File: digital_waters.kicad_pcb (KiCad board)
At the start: 4 copper layers, 100 x 45 mm, 118 parts, among them J1 Conn_Batt, J11 ESP32 [R], J16 ESP32 [L], J18 EZO Carrier Board, J2 Conn_Remote, J3 Conn_Sense_A, J4 Conn_Sense_B, J5 Conn_Illum, J6 Cal_in, U1 MCP3208, U10 ST485E, U12 DHT20, U13 TLV4387, U14 MCP1727-5002xSN, U15 TLV4387, U16 AP63200WU, U2 M24C02-FMN, U3 OPA197xD, U5 DIO5661ST6, U6 TPS22929D, U7 REF3040, U8 REF3025, U9 TLV2387DR

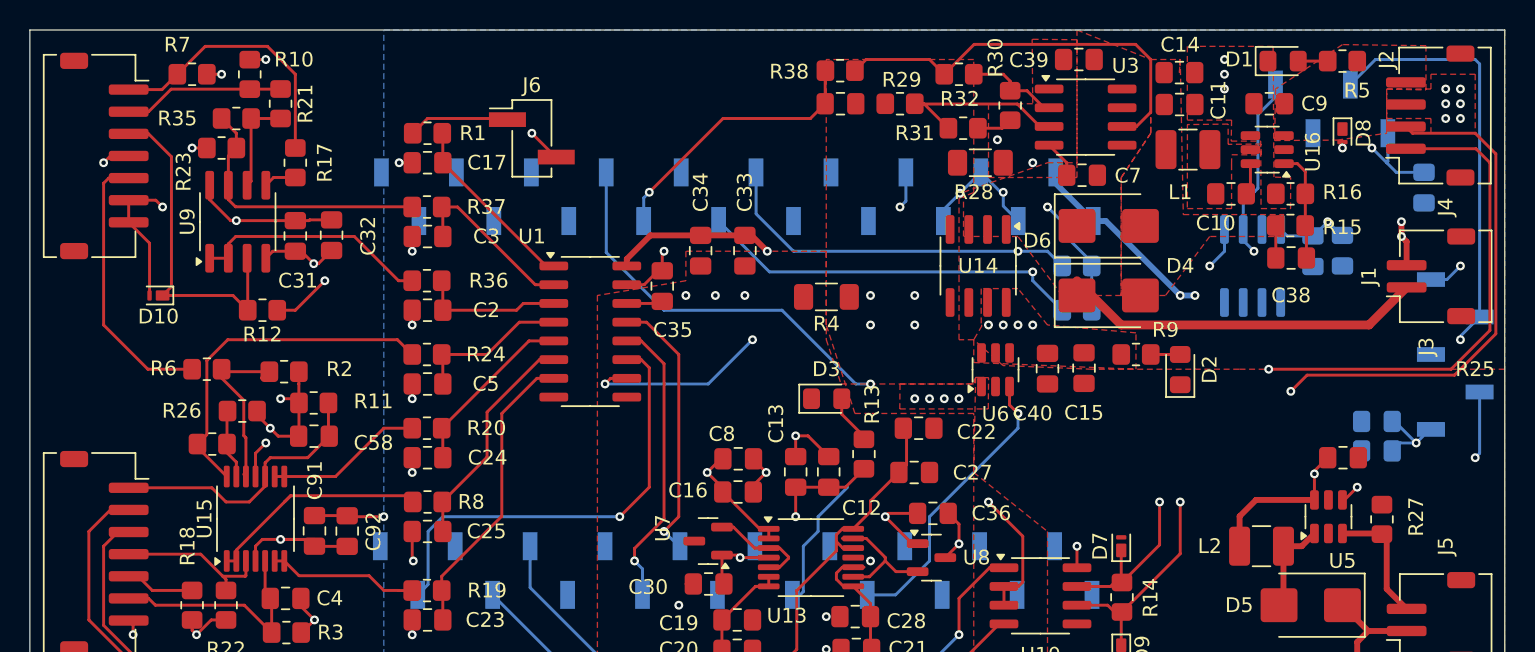
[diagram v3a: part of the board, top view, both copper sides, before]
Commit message: Maintenance update - Adding the EC isolation board schematic - Added a harness page for wireing module together
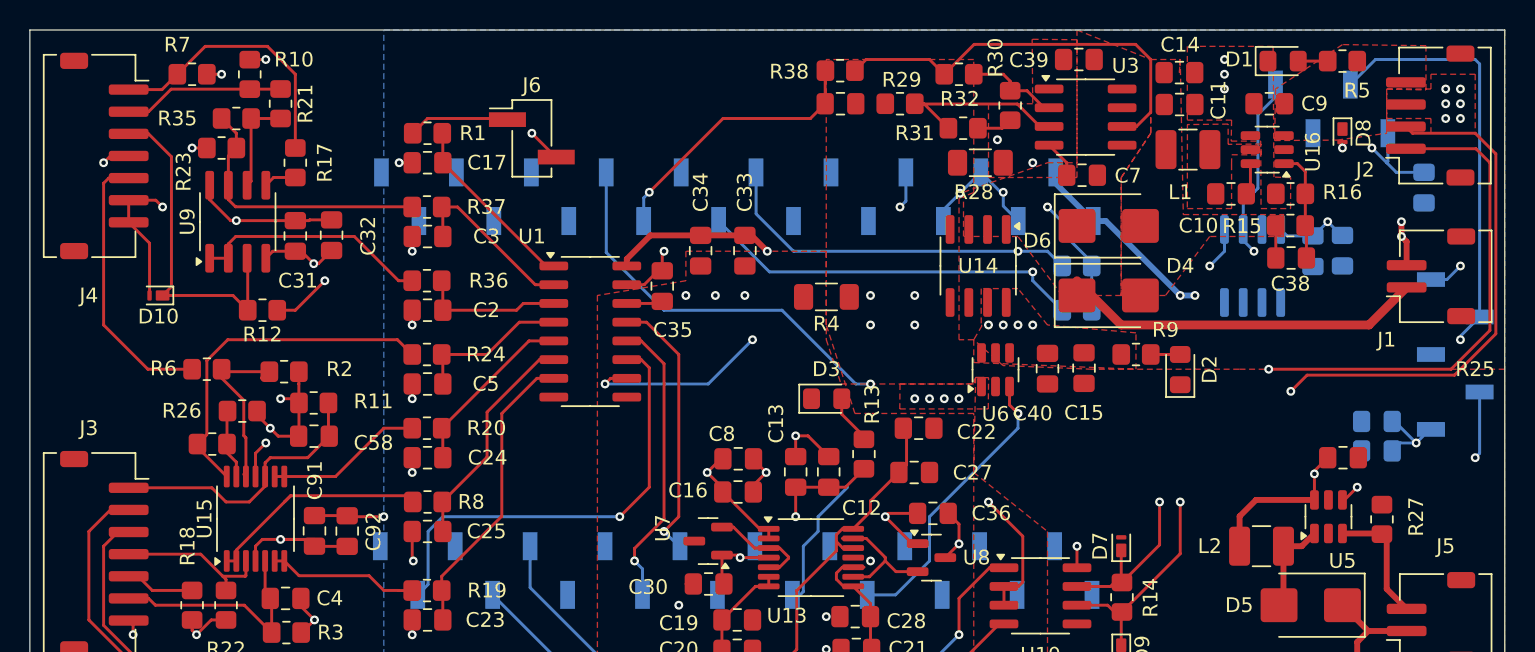
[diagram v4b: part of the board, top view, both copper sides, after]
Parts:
- C10: value 100nF -> 0.1u
- C9: value 10uF -> 10u
- R25: value 96k / 1% -> 91k / 1%
- R5: value 2k -> 2.2k
